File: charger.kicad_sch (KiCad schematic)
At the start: 38 parts

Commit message: Add barrel jack footprints
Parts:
- removed U?: LM75B, symbol Sensor_Temperature:LM75B
- added U?: LM75B, Package_SO:MSOP-8_3x3mm_P0.65mm, symbol Sensor_Temperature:LM75B
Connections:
- net +3V3: now also U?.8 (+Vs)
- net GND: now also U?.4 (GND), U?.5 (A2), U?.6 (A1), U?.7 (A0)
- net SCL: now also U?.2 (SCL)
- net SDA: now also U?.1 (SDA)
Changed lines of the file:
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@@
     (pin "2")
+  )
+  (symbol (lib_id "Sensor_Temperature:LM75B") (at 113.03 154.94 0) (unit 1)
+    (in_bom yes) (on_board yes) (fields_autoplaced)
+    (property "Reference" "U?" (id 0) (at 115.0494 141.0802 0)
+      (effects (font (size 1.27 1.27)) (justify left))
+    )
+    (property "Value" "LM75B" (id 1) (at 115.0494 143.6171 0)
+      (effects (font (size 1.27 1.27)) (justify left))
+    )
+    (property "Footprint" "Package_SO:MSOP-8_3x3mm_P0.65mm" (id 2) (at 113.03 154.94 0)
+      (effects (font (size 1.27 1.27)) hide)
+    )
+    (property "Datasheet" "http://www.ti.com/lit/ds/symlink/lm75b.pdf" (id 3) (at 113.03 154.94 0)
+      (effects (font (size 1.27 1.27)) hide)
+    )
+    (property "LCSC" "C2837470" (id 4) (at 113.03 154.94 0)
+      (effects (font (size 1.27 1.27)) hide)
+    )
+    (pin "1")
+    (pin "2")
+    (pin "3")
+    (pin "4")
+    (pin "5")
+    (pin "6")
+    (pin "7")
+    (pin "8")
   )
   (symbol (lib_id "Transistor_FET_DFN:AON7544") (at 62.23 69.85 90) (unit 1)
@@
     (pin "2")
   )
-  (symbol (lib_id "Sensor_Temperature:LM75B") (at 113.03 154.94 0) (unit 1)
-    (in_bom yes) (on_board yes) (fields_autoplaced)
-    (property "Reference" "U?" (id 0) (at 115.0494 141.0802 0)
-      (effects (font (size 1.27 1.27)) (justify left))
-    )
-    (property "Value" "LM75B" (id 1) (at 115.0494 143.6171 0)
-      (effects (font (size 1.27 1.27)) (justify left))
-    )
-    (property "Footprint" "" (id 2) (at 113.03 154.94 0)
-      (effects (font (size 1.27 1.27)) hide)
-    )
-    (property "Datasheet" "http://www.ti.com/lit/ds/symlink/lm75b.pdf" (id 3) (at 113.03 154.94 0)
-      (effects (font (size 1.27 1.27)) hide)
-    )
-    (pin "1")
-    (pin "2")
-    (pin "3")
-    (pin "4")
-    (pin "5")
-    (pin "6")
-    (pin "7")
-    (pin "8")
-  )
   (symbol (lib_id "power:GNDPWR") (at 142.24 115.57 0) (unit 1)

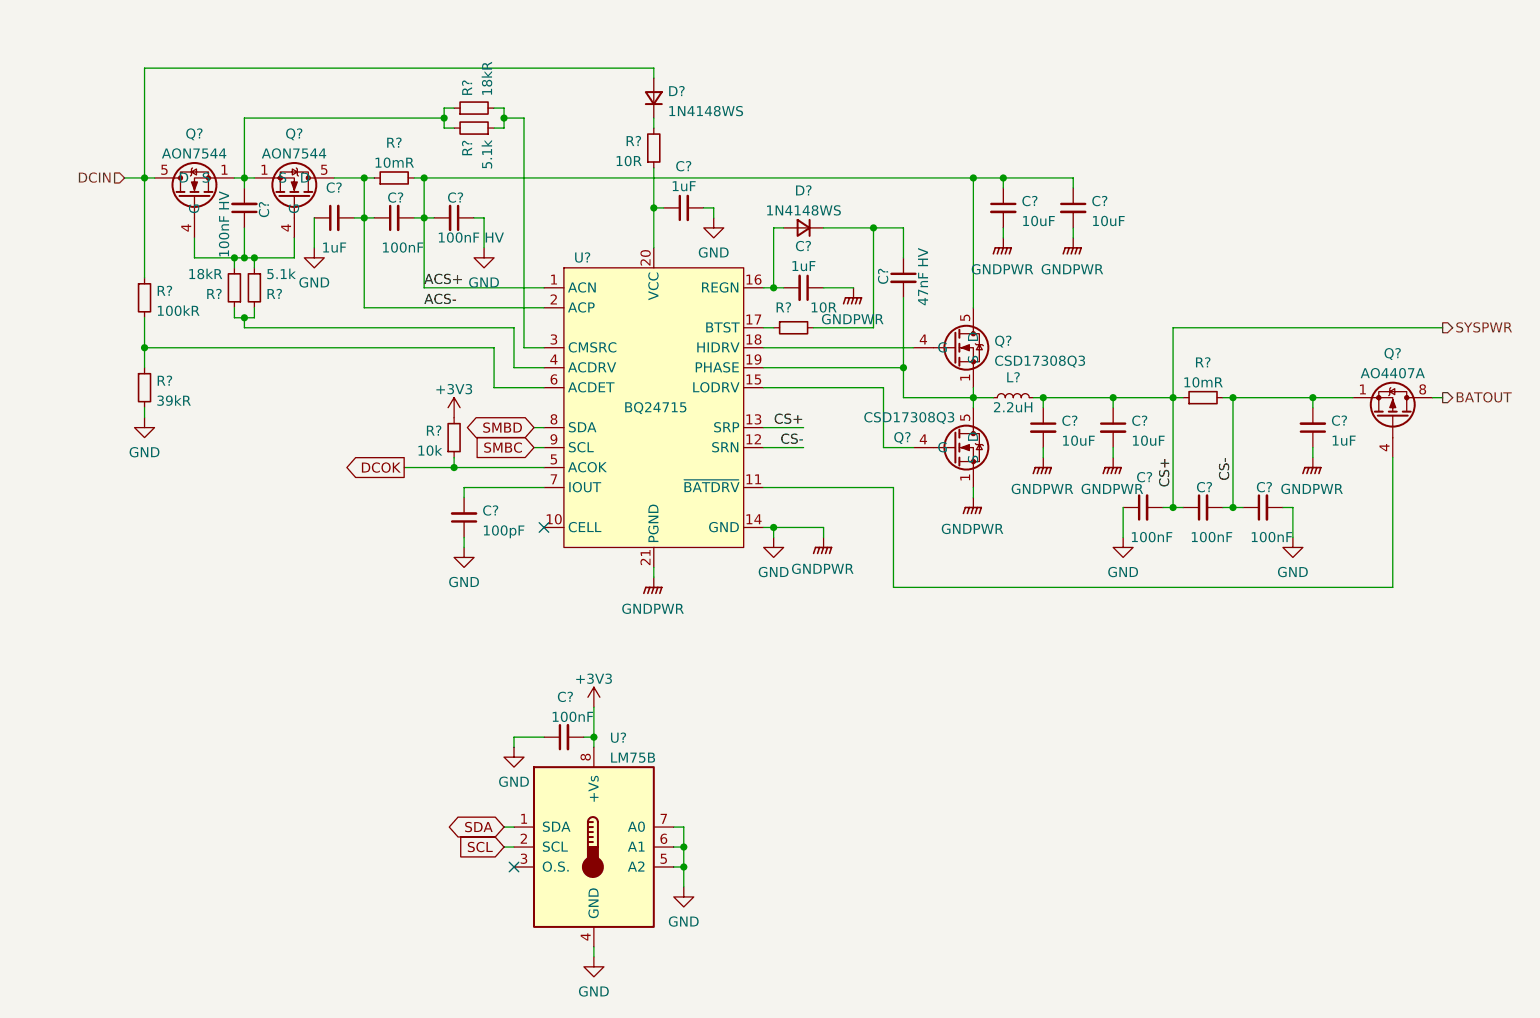
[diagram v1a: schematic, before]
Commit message: Add individually switchable outputs
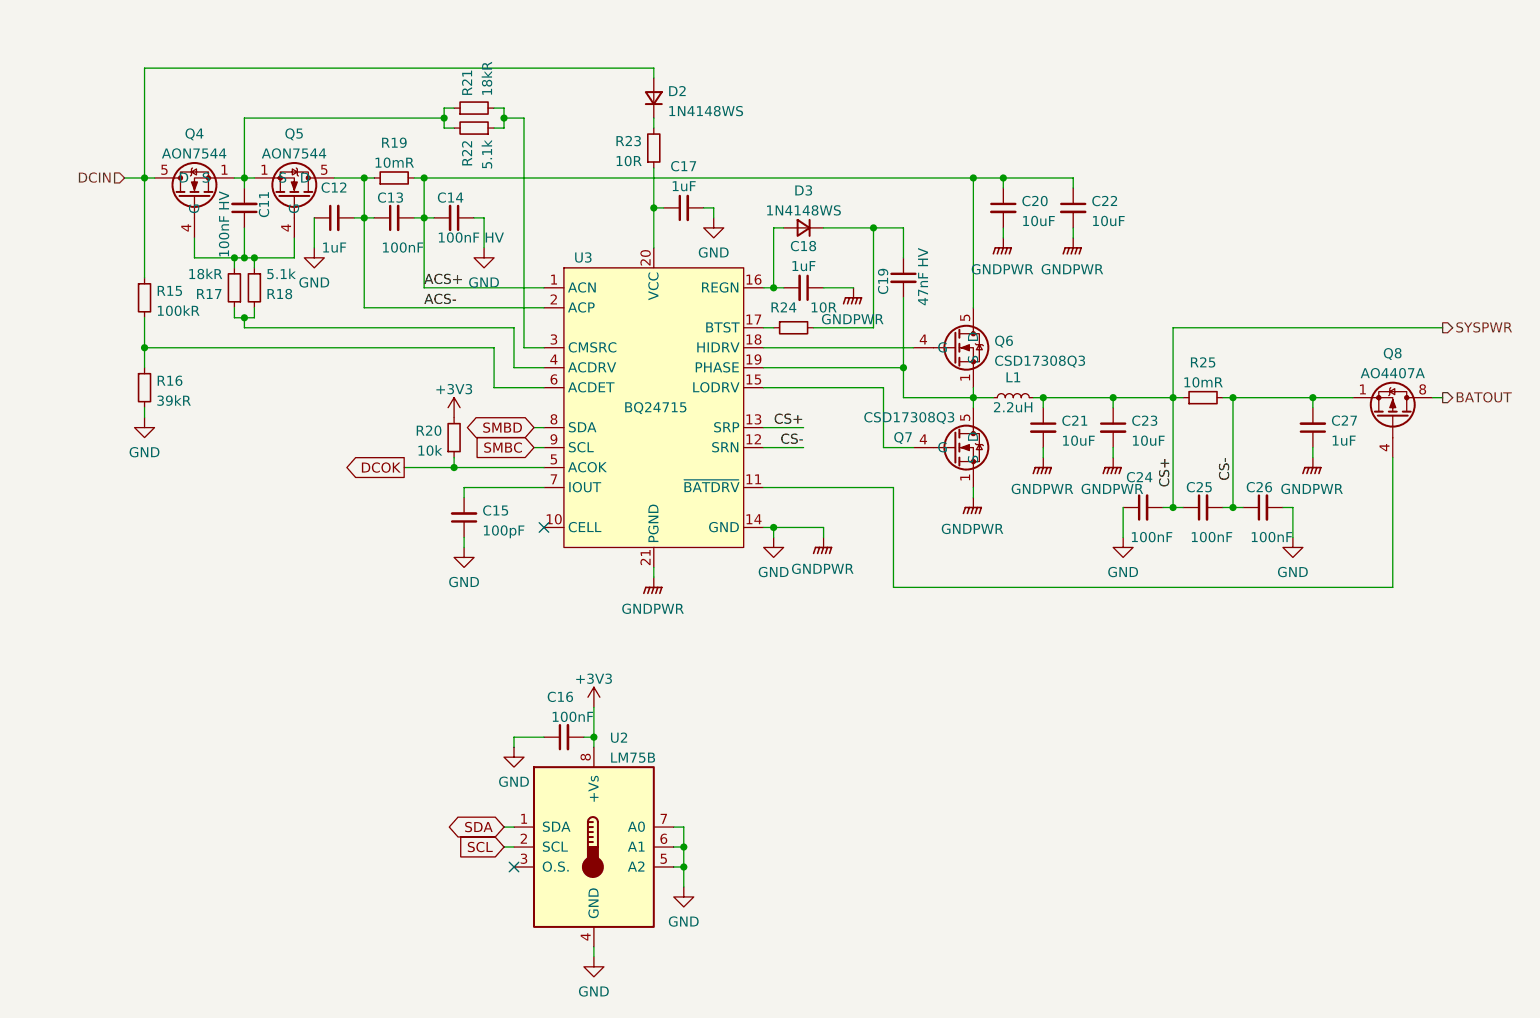
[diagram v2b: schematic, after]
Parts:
- gave numbers to parts that had none: 38

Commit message: Partial layout
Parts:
- added C104: 22nF, Capacitor_SMD:C_0402_1005Metric, symbol Device:C_Small
- added D17: YEL, LED_SMD:LED_0603_1608Metric, symbol Device:LED_Small
- added D18: RED, LED_SMD:LED_0603_1608Metric, symbol Device:LED_Small
- added D19: GRN, LED_SMD:LED_0603_1608Metric, symbol Device:LED_Small
- added Q26: 2N7002, Package_TO_SOT_SMD:SOT-23, symbol Transistor_FET:2N7002
- added R119, R121: 10k, Resistor_SMD:R_0402_1005Metric, symbol Device:R_Small
- added R120: 5.1k, Resistor_SMD:R_0402_1005Metric, symbol Device:R_Small
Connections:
- net +3V3: now also R120.1
- net ACS+: now also C12.2, C13.1, Q5.5 (D), Q5.6 (D), Q5.7 (D), Q5.8 (D), Q5.9 (D), R19.1, U3.2 (ACP); no longer C13.2, C14.2, C20.1, C22.1, Q6.5 (D), Q6.6 (D), Q6.7 (D), Q6.8 (D), Q6.9 (D), R19.2, U3.1 (ACN)
- net ACS-: now also C13.2, C14.2, C20.1, C22.1, Q6.5 (D), Q6.6 (D), Q6.7 (D), Q6.8 (D), Q6.9 (D), R19.2, U3.1 (ACN); no longer C12.2, C13.1, Q5.5 (D), Q5.6 (D), Q5.7 (D), Q5.8 (D), Q5.9 (D), R19.1, U3.2 (ACP)
- net DCIN: now also R119.2
- net DCOK: now also Q26.1 (G)
- net GND: now also C104.1, D17.1 (K), D19.1 (K), Q26.2 (S)
- net SYSPWR: now also R121.2
- net LX: now reaches C19.2, L1.1, Q6.1 (S), Q6.2 (S), Q6.3 (S), Q7.5 (D), Q7.6 (D), Q7.7 (D), Q7.8 (D), Q7.9 (D), U3.19 (PHASE)
- net INFETCOM: now reaches C11.2, Q4.1 (S), Q4.2 (S), Q4.3 (S), Q5.1 (S), Q5.2 (S), Q5.3 (S), R21.1, R22.2
- net at R15.2, R16.1, U3.6 (ACDET): now also C104.2
- new net: D19.2 (A), R121.1
- new net: D17.2 (A), R119.1
- new net: D18.1 (K), Q26.3 (D)
- new net: D18.2 (A), R120.2

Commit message: Fix footprint origins for JLC assembly
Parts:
- Q8: LCSC C16072 -> C35349
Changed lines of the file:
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@@
       (effects (font (size 1.27 1.27) italic) (justify left) hide)
     )
-    (property "Datasheet" "https://datasheet.lcsc.com/szlcsc/Alpha-Omega-Semicon-AOS-AO4407A_C16072.pdf" (id 3) (at 214.63 100.33 90)
+    (property "Datasheet" "https://datasheet.lcsc.com/szlcsc/Alpha-Omega-Semicon-AOS-AO4407A_C35349.pdf" (id 3) (at 214.63 100.33 90)
       (effects (font (size 1.27 1.27)) (justify left) hide)
     )
-    (property "LCSC" "C16072" (id 4) (at 214.63 100.33 0)
+    (property "LCSC" "C35349" (id 4) (at 214.63 100.33 0)
       (effects (font (size 1.27 1.27)) hide)
     )

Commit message: Fix incorrect AO447A partnumber
The previous partnumber was pointing to a N-Channel MOSFET.
Use a P-Channel one.
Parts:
- Q8: LCSC C35349 -> C167517
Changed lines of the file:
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@@
       (effects (font (size 1.27 1.27)) (justify left) hide)
     )
-    (property "LCSC" "C35349" (id 4) (at 214.63 100.33 0)
+    (property "LCSC" "C167517" (id 4) (at 214.63 100.33 0)
       (effects (font (size 1.27 1.27)) hide)
     )

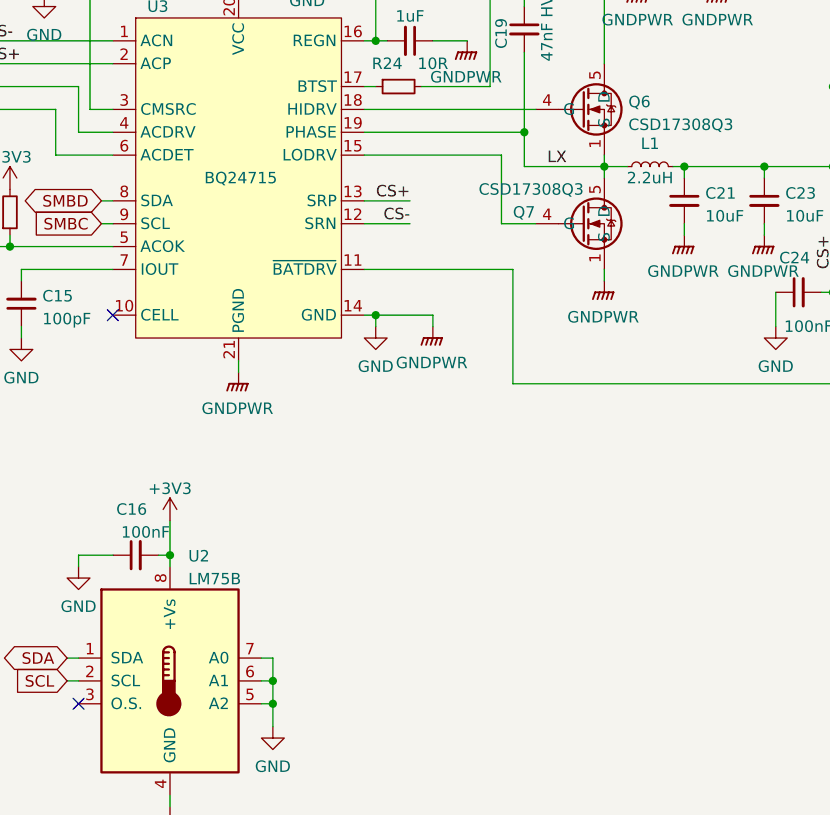
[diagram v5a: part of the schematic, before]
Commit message: Rev 1.0 bugfixes
Changes:
 - Replace DCOK-driven DC passthrough switch with ideal diode
 - Reduce INA219 series filter resistance to 1 ohm
 - Simplify debug USB power gating
 - Fix incorrect USB CC pullups
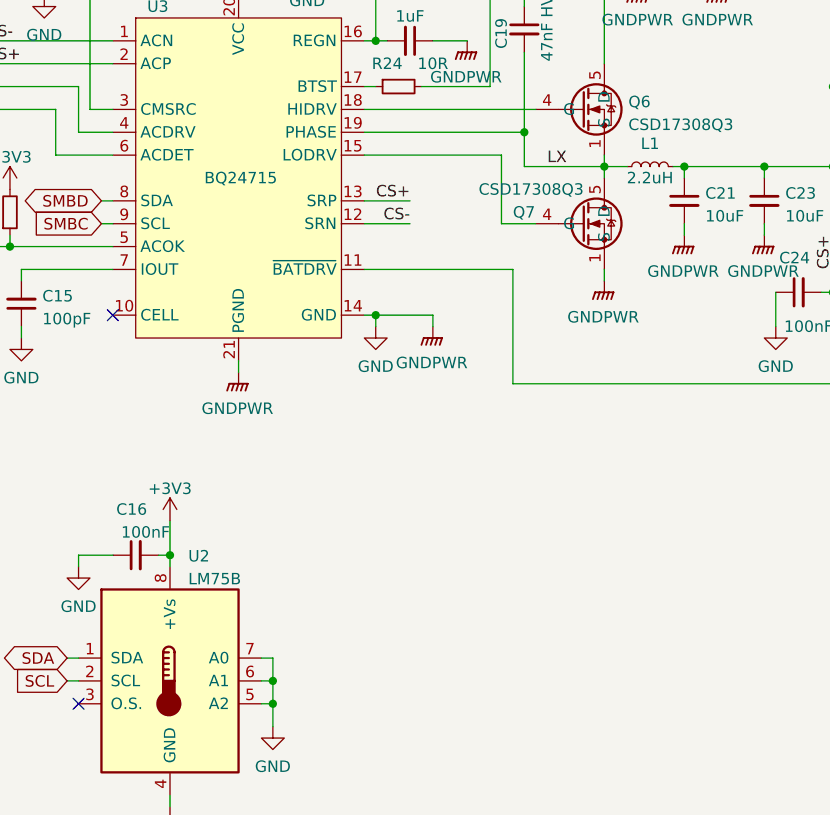
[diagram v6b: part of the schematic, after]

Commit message: Fix remaining RevB bugs
 - DNP Q13 by default to ensure uninterrupted power power delivery
 - Use lower resistance load resistors for DC step-up selftest
 - Add edge rails to support JLCPCB standard assembly

Unfortuantely JLCPCB does not seems to offer ESP32 WROOMs anymore for
economic PCBA. Thus edge-rails have been added to support standard PCBA.
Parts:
- D19: LCSC C72043 -> C2994781
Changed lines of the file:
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@@
       (effects (font (size 1.27 1.27)) hide)
     )
-    (property "LCSC" "C72043" (at 196.85 80.01 0)
+    (property "LCSC" "C2994781" (at 196.85 80.01 0)
       (effects (font (size 1.27 1.27)) hide)
     )
